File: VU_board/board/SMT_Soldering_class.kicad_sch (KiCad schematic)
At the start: 8 parts, among them J1 AVR-ISP-6, J2 USB_B_Micro, J3 Conn_01x04, U1 ATmega48PB-A

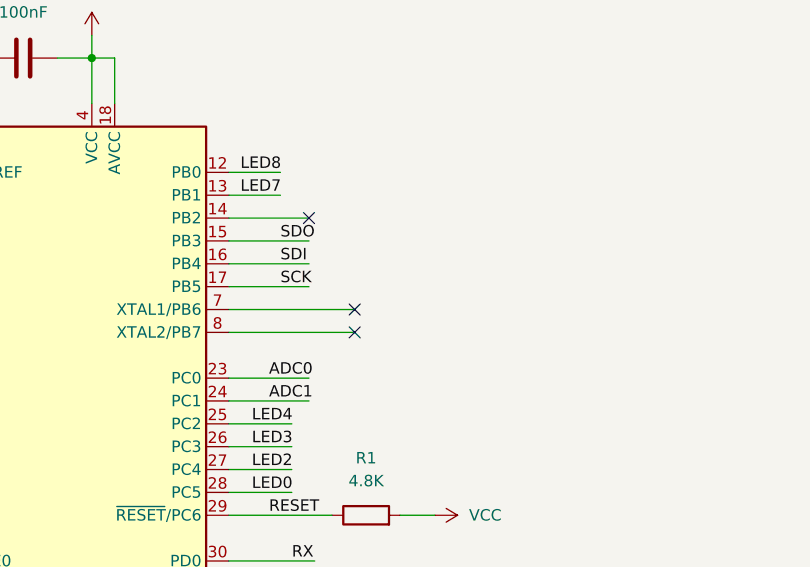
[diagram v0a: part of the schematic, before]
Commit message: added switch to PCB adding modes to firmware (for old version)
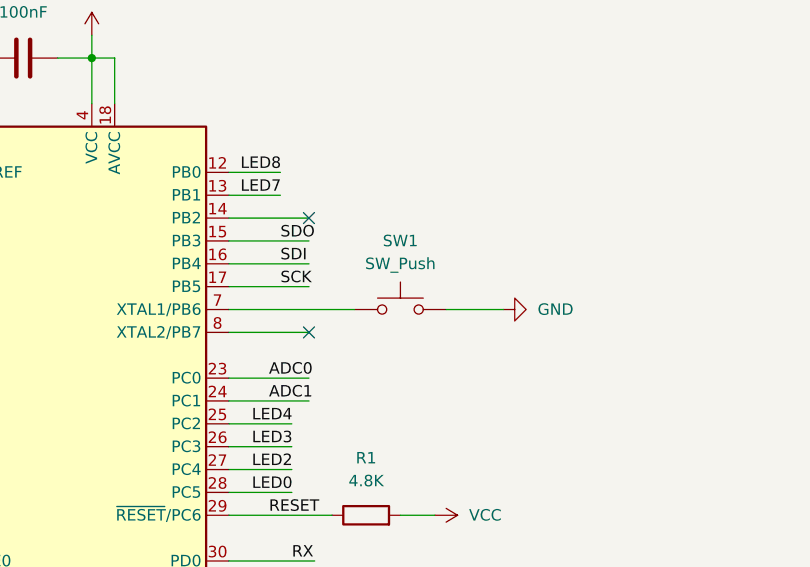
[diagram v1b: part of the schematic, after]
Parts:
- added SW1: SW_Push, Button_Switch_SMD:SW_Push_1P1T-SH_NO_CK_KMR2xxG, symbol Switch:SW_Push
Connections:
- net GND: now also SW1.1
- net at U1.7 (XTAL1/PB6): now also SW1.2
- no-connect marks 7 -> 6
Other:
- company: (none) -> NYC Resistor
- title: (none) -> SMT For You and Me, VU meter project board
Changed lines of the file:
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@@
 (kicad_sch (version 20211123) (generator eeschema)
   (paper "A4")
+  (title_block
+    (title "SMT For You and Me, VU meter project board")
+    (rev "2")
+    (company "NYC Resistor")
+    (comment 1 "COPY < IT > RIGHT")
+  )
   (junction (at 111.76 53.34) (diameter 0) (color 0 0 0 0)
   )
@@
   (no_connect (at 50.8 142.24))
   (no_connect (at 50.8 144.78))
-  (no_connect (at 140.97 81.28))
-  (no_connect (at 140.97 83.82))
   (no_connect (at 135.89 71.12))
+  (no_connect (at 135.89 83.82))
   (no_connect (at 40.64 152.4))
   (wire (pts (xy 82.55 66.04) (xy 86.36 66.04))
@@
     (stroke (width 0) (type default) (color 0 0 0 0))
   )
+  (wire (pts (xy 127 83.82) (xy 135.89 83.82))
+    (stroke (width 0) (type default) (color 0 0 0 0))
+  )
   (wire (pts (xy 111.76 53.34) (xy 111.76 58.42))
     (stroke (width 0) (type default) (color 0 0 0 0))
@@
     (stroke (width 0) (type default) (color 0 0 0 0))
   )
-  (wire (pts (xy 127 83.82) (xy 140.97 83.82))
-    (stroke (width 0) (type default) (color 0 0 0 0))
-  )
   (wire (pts (xy 198.12 33.02) (xy 203.835 33.02))
     (stroke (width 0) (type default) (color 0 0 0 0))
@@
   )
   (wire (pts (xy 198.12 93.98) (xy 203.835 93.98))
+    (stroke (width 0) (type default) (color 0 0 0 0))
+  )
+  (wire (pts (xy 151.13 81.28) (xy 157.48 81.28))
     (stroke (width 0) (type default) (color 0 0 0 0))
   )
@@
     )
     (pin "1")
+  )
+  (symbol (lib_id "Switch:SW_Push") (at 146.05 81.28 0) (mirror y) (unit 1)
+    (in_bom yes) (on_board yes) (fields_autoplaced)
+    (property "Reference" "SW1" (id 0) (at 146.05 73.66 0))
+    (property "Value" "SW_Push" (id 1) (at 146.05 76.2 0))
+    (property "Footprint" "Button_Switch_SMD:SW_Push_1P1T-SH_NO_CK_KMR2xxG" (id 2) (at 146.05 76.2 0)
+      (effects (font (size 1.27 1.27)) hide)
+    )
+    (property "Datasheet" "~" (id 3) (at 146.05 76.2 0)
+      (effects (font (size 1.27 1.27)) hide)
+    )
+    (pin "1")
+    (pin "2")
   )
   (symbol (lib_id "Connector_Generic:Conn_01x04") (at 85.09 162.56 0) (unit 1)
@@
     (pin "9")
   )
+  (symbol (lib_id "power:GND") (at 157.48 81.28 90) (unit 1)
+    (in_bom yes) (on_board yes) (fields_autoplaced)
+    (property "Reference" "#PWR011" (id 0) (at 163.83 81.28 0)
+      (effects (font (size 1.27 1.27)) hide)
+    )
+    (property "Value" "GND" (id 1) (at 161.29 81.2799 90)
+      (effects (font (size 1.27 1.27)) (justify right))
+    )
+    (property "Footprint" "" (id 2) (at 157.48 81.28 0)
+      (effects (font (size 1.27 1.27)) hide)
+    )
+    (property "Datasheet" "" (id 3) (at 157.48 81.28 0)
+      (effects (font (size 1.27 1.27)) hide)
+    )
+    (pin "1")
+  )
   (symbol (lib_id "Device:R") (at 142.24 104.14 90) (unit 1)
     (in_bom yes) (on_board yes) (fields_autoplaced)
@@
       (reference "#PWR010") (unit 1) (value "GND") (footprint "")
     )
+    (path "/8d2552e4-162e-48f6-ae36-61075f65c1d4"
+      (reference "#PWR011") (unit 1) (value "GND") (footprint "")
+    )
     (path "/28567c43-840a-4cfa-a763-f2f8d9bcb25b"
       (reference "#PWR012") (unit 1) (value "VCC") (footprint "")
@@
       (reference "R17") (unit 1) (value "R") (footprint "Resistor_SMD:R_0805_2012Metric_Pad1.20x1.40mm_HandSolder")
     )
+    (path "/104404fd-358b-4a72-9c7d-7be74d74f7fd"
+      (reference "SW1") (unit 1) (value "SW_Push") (footprint "Button_Switch_SMD:SW_Push_1P1T-SH_NO_CK_KMR2xxG")
+    )
     (path "/bd966186-9aa3-4fe2-9fee-d28c754ccc6c/546a0c6c-285e-471f-b1d8-dda44d7dc824"
